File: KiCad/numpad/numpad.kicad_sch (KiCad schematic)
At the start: 40 parts, among them J12 Conn_01x04_Pin, SW10 Cherry Switch Single, SW11 Cherry Switch Single, SW12 Cherry Switch Single, SW13 Cherry Switch Single, SW3 Cherry Switch Single, SW4 Cherry Switch Single, SW5 Cherry Switch Single, SW6 Cherry Switch Single, SW7 Cherry Switch Single, SW9 Cherry Switch Single, U8 TL431D, U9 LT1632

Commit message: schematics finished
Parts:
- D1: footprint (none) -> Diode_SMD:D_0603_1608Metric
- R21: value 330R -> 4k7
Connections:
- net NumpadOut_toADC renamed NUMPAD_A_OUT
- net VREF_measback renamed NUMPAD_VREF
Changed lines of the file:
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@@
 	(generator_version "9.0")
 	(paper "A4")
-	(text "Visszajelző LED\n\n"
-		(exclude_from_sim no)
-		(at 208.026 64.516 0)
-		(effects
-			(font
-				(size 1.27 1.27)
-			)
-			(justify left top)
+	(rectangle
+		(start 207.645 12.319)
+		(end 229.2349 17.399)
+		(stroke
+			(width 0)
+			(type solid)
+			(color 255 229 191 1)
+		)
+		(fill
+			(type color)
+			(color 255 153 0 1)
 		)
 	)
-	(text "Referenciafeszültség előállítása"
+	(rectangle
+		(start 12.065 65.024)
+		(end 79.3749 70.104)
+		(stroke
+			(width 0)
+			(type solid)
+			(color 255 229 191 1)
+		)
+		(fill
+			(type color)
+			(color 255 153 0 1)
+		)
+	)
+	(rectangle
+		(start 207.518 109.601)
+		(end 243.0779 114.681)
+		(stroke
+			(width 0)
+			(type solid)
+			(color 255 229 191 1)
+		)
+		(fill
+			(type color)
+			(color 255 153 0 1)
+		)
+	)
+	(rectangle
+		(start 207.518 63.881)
+		(end 237.9979 68.961)
+		(stroke
+			(width 0)
+			(type solid)
+			(color 255 229 191 1)
+		)
+		(fill
+			(type color)
+			(color 255 153 0 1)
+		)
+	)
+	(rectangle
+		(start 12.7 127.254)
+		(end 71.1199 132.334)
+		(stroke
+			(width 0)
+			(type solid)
+			(color 255 229 191 1)
+		)
+		(fill
+			(type color)
+			(color 255 153 0 1)
+		)
+	)
+	(rectangle
+		(start 93.345 12.319)
+		(end 109.8549 17.399)
+		(stroke
+			(width 0)
+			(type solid)
+			(color 255 229 191 1)
+		)
+		(fill
+			(type color)
+			(color 255 153 0 1)
+		)
+	)
+	(rectangle
+		(start 12.7 12.319)
+		(end 74.9299 17.399)
+		(stroke
+			(width 0)
+			(type solid)
+			(color 255 229 191 1)
+		)
+		(fill
+			(type color)
+			(color 255 153 0 1)
+		)
+	)
+	(text "Visszajelző LED\n"
 		(exclude_from_sim no)
-		(at 13.97 13.97 0)
+		(at 222.885 66.675 0)
 		(effects
 			(font
-				(size 1.27 1.27)
+				(size 2.54 2.54)
+				(thickness 0.508)
+				(bold yes)
+				(color 255 255 255 1)
 			)
-			(justify left top)
 		)
 	)
-	(text "Numpad"
+	(text "Referenciafeszültség előállítása"
 		(exclude_from_sim no)
-		(at 98.806 14.732 0)
+		(at 43.815 15.24 0)
 		(effects
 			(font
-				(size 1.27 1.27)
+				(size 2.54 2.54)
+				(thickness 0.508)
+				(bold yes)
+				(color 255 255 255 1)
 			)
 		)
 	)
-	(text "Opamp tápellátás"
+	(text "Referenciafeszültség visszamérése"
 		(exclude_from_sim no)
-		(at 208.28 110.49 0)
+		(at 45.72 67.945 0)
 		(effects
 			(font
-				(size 1.27 1.27)
+				(size 2.54 2.54)
+				(thickness 0.508)
+				(bold yes)
+				(color 255 255 255 1)
 			)
-			(justify left top)
 		)
 	)
-	(text "Referenciafeszültség visszamérése"
+	(text "Numpadkimenet visszamérése"
 		(exclude_from_sim no)
-		(at 13.97 66.04 0)
+		(at 41.91 130.175 0)
 		(effects
 			(font
-				(size 1.27 1.27)
+				(size 2.54 2.54)
+				(thickness 0.508)
+				(bold yes)
+				(color 255 255 255 1)
 			)
-			(justify left top)
 		)
 	)
-	(text "Numpadkimenet visszamérése"
+	(text "Numpad"
 		(exclude_from_sim no)
-		(at 12.954 128.016 0)
+		(at 101.6 15.24 0)
 		(effects
 			(font
-				(size 1.27 1.27)
+				(size 2.54 2.54)
+				(thickness 0.508)
+				(bold yes)
+				(color 255 255 255 1)
 			)
-			(justify left top)
 		)
 	)
@@
 	(text "Csatlakozó"
 		(exclude_from_sim no)
-		(at 208.28 13.97 0)
+		(at 218.44 15.24 0)
 		(effects
 			(font
-				(size 1.27 1.27)
+				(size 2.54 2.54)
+				(thickness 0.508)
+				(bold yes)
+				(color 255 255 255 1)
+			)
+		)
+	)
+	(text "Opamp tápellátás"
+		(exclude_from_sim no)
+		(at 225.425 112.395 0)
+		(effects
+			(font
+				(size 2.54 2.54)
+				(thickness 0.508)
+				(bold yes)
+				(color 255 255 255 1)
 			)
-			(justify left top)
 		)
 	)
@@
 		)
 	)
-	(polyline
+	(wire
 		(pts
-			(xy 207.01 12.7) (xy 207.01 165.1)
+			(xy 147.32 31.75) (xy 158.75 31.75)
 		)
 		(stroke
@@
 	(wire
 		(pts
-			(xy 147.32 31.75) (xy 158.75 31.75)
+			(xy 184.15 31.75) (xy 187.96 31.75)
 		)
 		(stroke
@@
 		)
 	)
-	(wire
+	(polyline
 		(pts
-			(xy 184.15 31.75) (xy 187.96 31.75)
+			(xy 92.71 12.065) (xy 92.71 198.12)
 		)
 		(stroke
-			(width 0)
-			(type default)
+			(width 0.762)
+			(type solid)
+			(color 255 153 0 1)
 		)
 	)
@@
 		)
 	)
+	(polyline
+		(pts
+			(xy 207.01 12.065) (xy 207.01 165.735)
+		)
+		(stroke
+			(width 0.762)
+			(type solid)
+			(color 255 153 0 1)
+		)
+	)
 	(wire
 		(pts
@@
 		)
 	)
+	(polyline
+		(pts
+			(xy 207.01 109.22) (xy 285.115 109.22)
+		)
+		(stroke
+			(width 0.762)
+			(type solid)
+			(color 255 153 0 1)
+		)
+	)
 	(wire
 		(pts
@@
 		)
 	)
-	(wire
+	(polyline
 		(pts
-			(xy 20.32 25.4) (xy 20.32 27.94)
+			(xy 12.065 64.77) (xy 92.71 64.77)
 		)
 		(stroke
-			(width 0)
-			(type default)
+			(width 0.762)
+			(type solid)
+			(color 255 153 0 1)
 		)
 	)
 	(wire
 		(pts
-			(xy 120.65 92.71) (xy 120.65 95.25)
+			(xy 20.32 25.4) (xy 20.32 27.94)
 		)
 		(stroke
@@
 	(wire
 		(pts
-			(xy 120.65 120.65) (xy 137.16 120.65)
+			(xy 120.65 92.71) (xy 120.65 95.25)
 		)
 		(stroke
@@
 		)
 	)
-	(polyline
+	(wire
 		(pts
-			(xy 92.71 12.7) (xy 92.71 196.85)
+			(xy 120.65 120.65) (xy 137.16 120.65)
 		)
 		(stroke
@@
 		)
 	)
+	(polyline
+		(pts
+			(xy 12.065 126.365) (xy 92.71 126.365)
+		)
+		(stroke
+			(width 0.762)
+			(type solid)
+			(color 255 153 0 1)
+		)
+	)
 	(wire
 		(pts
@@
 		)
 	)
-	(polyline
-		(pts
-			(xy 12.7 127) (xy 92.71 127)
-		)
-		(stroke
-			(width 0)
-			(type default)
-		)
-	)
 	(wire
 		(pts
@@
 		)
 	)
-	(polyline
-		(pts
-			(xy 92.71 99.06) (xy 92.71 196.85)
-		)
-		(stroke
-			(width 0)
-			(type default)
-		)
-	)
 	(wire
 		(pts
@@
 		)
 	)
-	(polyline
-		(pts
-			(xy 12.7 64.77) (xy 92.71 64.77)
-		)
-		(stroke
-			(width 0)
-			(type default)
-		)
-	)
 	(wire
 		(pts
@@
 		)
 	)
-	(wire
+	(polyline
 		(pts
-			(xy 120.65 133.35) (xy 137.16 133.35)
+			(xy 207.01 63.5) (xy 285.115 63.5)
 		)
 		(stroke
-			(width 0)
-			(type default)
+			(width 0.762)
+			(type solid)
+			(color 255 153 0 1)
 		)
 	)
 	(wire
 		(pts
-			(xy 35.56 91.44) (xy 35.56 99.06)
+			(xy 120.65 133.35) (xy 137.16 133.35)
 		)
 		(stroke
@@
 	(wire
 		(pts
-			(xy 120.65 105.41) (xy 120.65 107.95)
+			(xy 35.56 91.44) (xy 35.56 99.06)
 		)
 		(stroke
@@
 		)
 	)
-	(polyline
+	(wire
 		(pts
-			(xy 207.01 63.5) (xy 285.115 63.5)
+			(xy 120.65 105.41) (xy 120.65 107.95)
 		)
 		(stroke
@@
 		)
 	)
-	(polyline
-		(pts
-			(xy 207.01 109.22) (xy 284.48 109.22)
-		)
-		(stroke
-			(width 0)
-			(type default)
-		)
-	)
 	(wire
 		(pts
@@
 		)
 	)
-	(label "NumpadOut_toADC"
+	(label "NUMPAD_A_OUT"
 		(at 252.73 43.18 0)
 		(effects
@@
 		)
 	)
-	(label "VREF_measback"
+	(label "NUMPAD_VREF"
 		(at 252.73 40.64 0)
 		(effects
@@
 		)
 	)
-	(label "VREF_measback"
+	(label "NUMPAD_VREF"
 		(at 64.77 90.17 0)
 		(effects
@@
 		)
 	)
-	(label "NumpadOut_toADC"
+	(label "NUMPAD_A_OUT"
 		(at 64.77 154.94 0)
 		(effects
@@
 			)
 		)
-		(property "Footprint" ""
+		(property "Footprint" "Diode_SMD:D_0603_1608Metric"
 			(at 243.84 93.98 0)
 			(effects
@@
 			)
 		)
-		(property "Value" "330R"
+		(property "Value" "4k7"
 			(at 246.38 85.0899 0)
 			(effects

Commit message: PCB designs started
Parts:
- added H1, H2, H3, H4: MountingHole, MountingHole:MountingHole_3.2mm_M3, symbol Mechanical:MountingHole
- renumbered C3 to C2, C2 to C3, J12 to J1, R12 to R1, R2 to R10, R3 to R11, R4 to R12, R5 to R13, R6 to R14, R7 to R15, R8 to R16, R9 to R17, R11 to R18, R10 to R19, R13 to R2, R18 to R20, R14 to R3, R16 to R4, R19 to R5, R17 to R6, R20 to R7, R15 to R8, R1 to R9, SW3 to SW1, SW12 to SW10, SW4 to SW2, SW5 to SW3, SW7 to SW4, SW9 to SW5, SW11 to SW6, SW13 to SW7, SW6 to SW8, SW10 to SW9, U9 to U1, U8 to U2

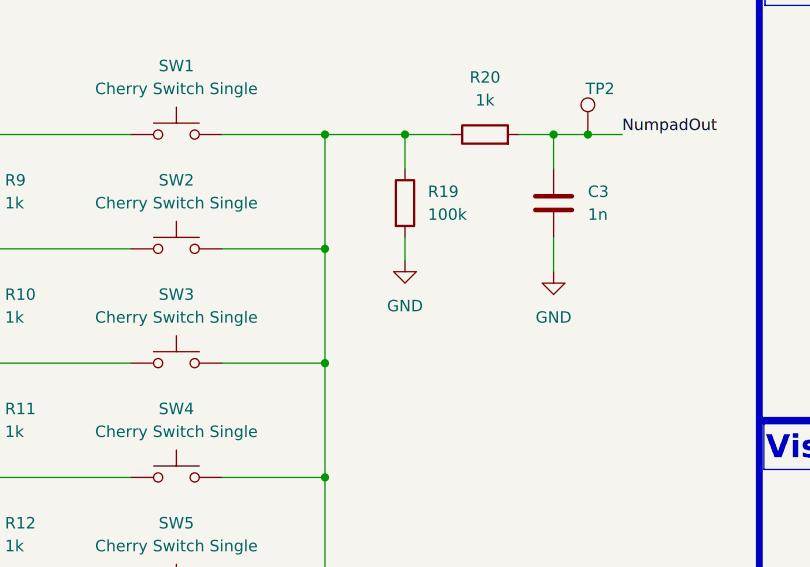
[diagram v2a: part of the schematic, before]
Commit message: documentation, OLED demo, BOM
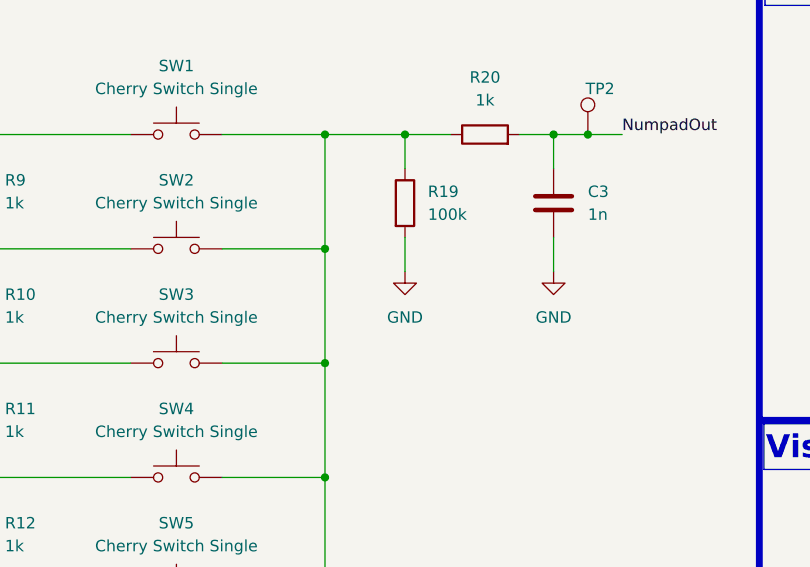
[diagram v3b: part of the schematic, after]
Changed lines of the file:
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@@
 	(wire
 		(pts
-			(xy 167.64 43.18) (xy 167.64 45.72)
+			(xy 167.64 43.18) (xy 167.64 46.99)
 		)
 		(stroke
@@
 	(symbol
 		(lib_id "power:GND")
-		(at 167.64 45.72 0)
+		(at 167.64 46.99 0)
 		(unit 1)
 		(exclude_from_sim no)
@@
 		(fields_autoplaced yes)
 		(property "Reference" "#PWR07"
+			(at 167.64 53.34 0)
+			(effects
+				(font
+					(size 1.27 1.27)
+				)
+				(hide yes)
+			)
+		)
+		(property "Value" "GND"
 			(at 167.64 52.07 0)
 			(effects
@@
 					(size 1.27 1.27)
 				)
-				(hide yes)
-			)
-		)
-		(property "Value" "GND"
-			(at 167.64 50.8 0)
-			(effects
-				(font
-					(size 1.27 1.27)
-				)
 			)
 		)
 		(property "Footprint" ""
-			(at 167.64 45.72 0)
+			(at 167.64 46.99 0)
 			(effects
 				(font
@@
 		)
 		(property "Datasheet" ""
-			(at 167.64 45.72 0)
+			(at 167.64 46.99 0)
 			(effects
 				(font
@@
 		)
 		(property "Description" "Power symbol creates a global label with name \"GND\" , ground"
-			(at 167.64 45.72 0)
-			(effects
-				(font
+			(at 167.64 46.99 0)
+			(effects
+				(font

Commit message: exports
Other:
- title: (none) -> Numerikus billentyűzet
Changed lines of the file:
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@@
 	(generator_version "9.0")
 	(paper "A4")
+	(title_block
+		(title "Numerikus billentyűzet")
+	)
 	(rectangle
 		(start 207.645 12.319)
